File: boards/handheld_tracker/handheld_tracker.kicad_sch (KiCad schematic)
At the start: 0 parts

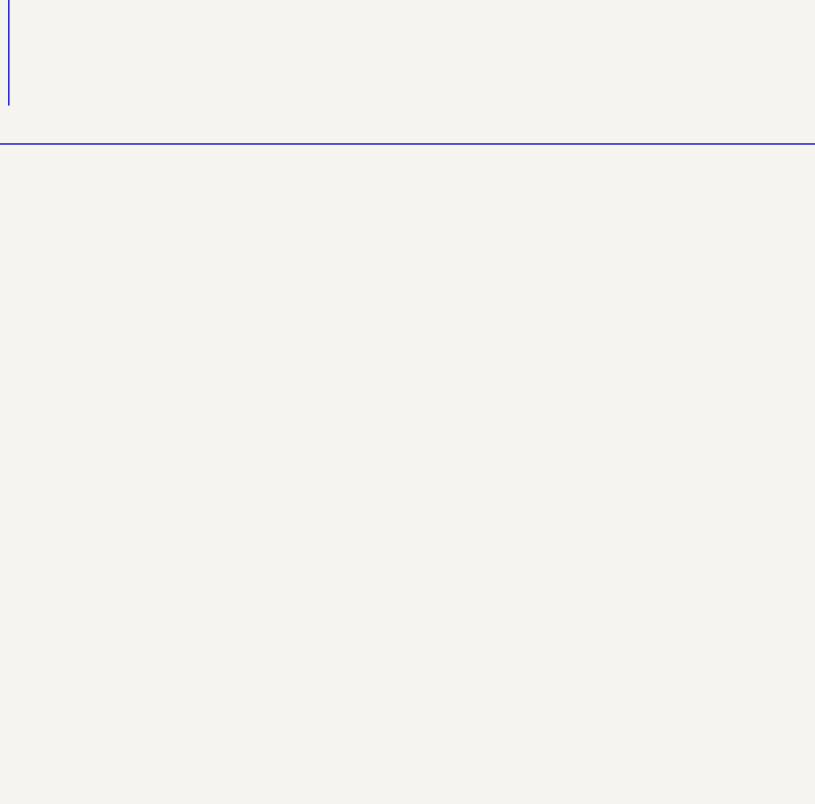
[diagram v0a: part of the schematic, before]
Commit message: created section for test pins
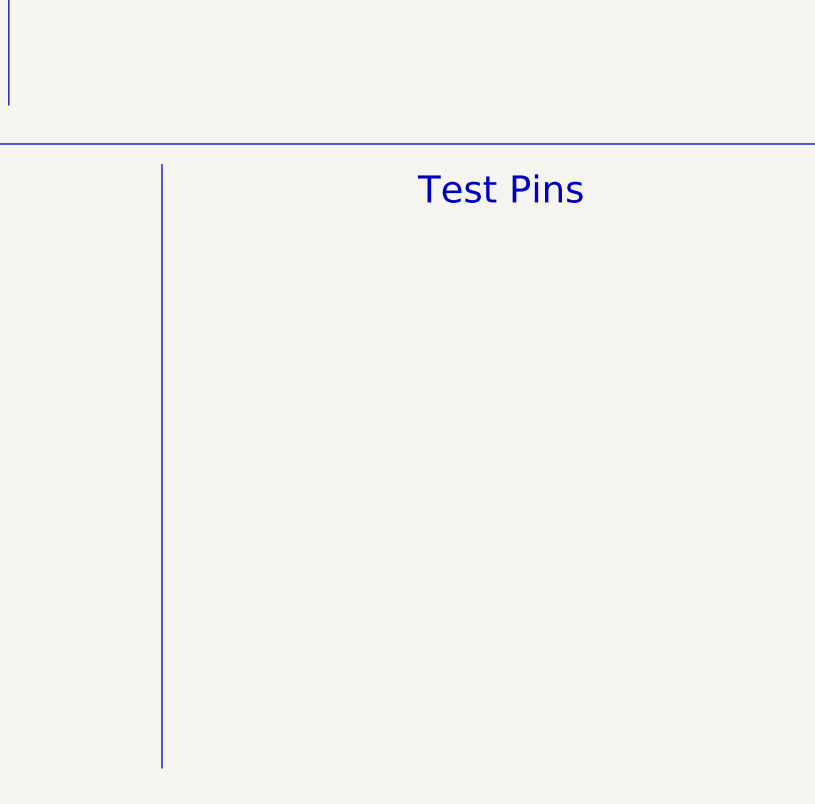
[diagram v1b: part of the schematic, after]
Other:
- note added: "Test Pins"
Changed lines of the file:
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@@
+    (stroke (width 0) (type default) (color 0 0 0 0))
+  )
+  (polyline (pts (xy 184.658 98.806) (xy 184.658 165.862))
     (stroke (width 0) (type default) (color 0 0 0 0))
   )
@@
     (effects (font (size 3 3)) (justify left bottom))
   )
+  (text "Test Pins" (at 213.106 103.632 0)
+    (effects (font (size 3 3)) (justify left bottom))
+  )

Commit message: added notes
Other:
- note added: "- I2C lines - SPI lines - Input voltage - Regulated voltage - GND"
- note added: "Likely needs to be modified to account for MCU change...may need 5V to power larger MCU"
- note added: "Make heirarchy...for buttons & screen"
- note added: "SAM-M8Q"
- note added: "TBD"
- note added: "Transceiver + SMA antenna connector"
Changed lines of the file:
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@@
     (effects (font (size 3 3)) (justify left bottom))
+  )
+  (text "Likely needs to be modified to account for MCU \nchange...may need 5V to power larger MCU"
+    (at 26.67 114.554 0)
+    (effects (font (size 1.27 1.27)) (justify left bottom))
   )
   (text "Test Pins" (at 213.106 103.632 0)
@@
     (effects (font (size 3 3)) (justify left bottom))
   )
+  (text "Transceiver + SMA antenna connector" (at 194.818 49.022 0)
+    (effects (font (size 1.27 1.27)) (justify left bottom))
+  )
+  (text "SAM-M8Q" (at 113.538 50.038 0)
+    (effects (font (size 1.27 1.27)) (justify left bottom))
+  )
+  (text "- I2C lines\n- SPI lines\n- Input voltage\n- Regulated voltage\n- GND"
+    (at 221.488 128.016 0)
+    (effects (font (size 1.27 1.27)) (justify left bottom))
+  )
+  (text "TBD" (at 42.672 52.324 0)
+    (effects (font (size 1.27 1.27)) (justify left bottom))
+  )
   (text "Power" (at 44.196 104.14 0)
     (effects (font (size 3 3)) (justify left bottom))
   )
+  (text "Make heirarchy...for buttons & screen" (at 118.618 125.73 0)
+    (effects (font (size 1.27 1.27)) (justify left bottom))
+  )
   (sheet_instances

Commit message: added sensor and MCU
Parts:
- added U1: SAM-M8Q, RF_GPS:ublox_SAM-M8Q, symbol RF_GPS:SAM-M8Q
- added U2: RFM96W-433S2, symbol RF_Module:RFM96W-433S2
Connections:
- new net: U1.1 (GND), U1.10 (GND), U1.11 (GND), U1.15 (GND), U1.16 (GND), U1.20 (GND), U1.4 (GND), U1.5 (GND), U1.6 (GND)
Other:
- added sheet mcu (mcu.kicad_sch)
- added sheet user_interface (user_interface.kicad_sch)
- note removed: "Likely needs to be modified to account for MCU change...may need 5V to power larger MCU"
- note removed: "Make heirarchy...for buttons & screen"
- note removed: "SAM-M8Q"
- note removed: "TBD"
- note removed: "Transceiver + SMA antenna connector"
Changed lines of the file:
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@@
     (stroke (width 0) (type default) (color 0 0 0 0))
   )
-  (text "MCU" (at 46.228 25.4 0)
+  (text "MCU" (at 45.72 25.4 0)
     (effects (font (size 3 3)) (justify left bottom))
   )
-  (text "Likely needs to be modified to account for MCU \nchange...may need 5V to power larger MCU"
-    (at 26.67 114.554 0)
+  (text "Test Pins" (at 214.63 104.14 0)
+    (effects (font (size 3 3)) (justify left bottom))
+  )
+  (text "User Interface" (at 114.3 105.41 0)
+    (effects (font (size 3 3)) (justify left bottom))
+  )
+  (text "Sensors" (at 118.11 24.13 0)
+    (effects (font (size 3 3)) (justify left bottom))
+  )
+  (text "Communication" (at 189.23 26.67 0)
+    (effects (font (size 3 3)) (justify left bottom))
+  )
+  (text "- I2C lines\n- SPI lines\n- Input voltage\n- Regulated voltage\n- GND"
+    (at 220.98 128.27 0)
     (effects (font (size 1.27 1.27)) (justify left bottom))
   )
-  (text "Test Pins" (at 213.106 103.632 0)
+  (text "Power" (at 44.45 105.41 0)
     (effects (font (size 3 3)) (justify left bottom))
   )
-  (text "User Interface" (at 114.3 104.394 0)
-    (effects (font (size 3 3)) (justify left bottom))
+  (symbol (lib_id "RF_Module:RFM96W-433S2") (at 213.36 52.07 0) (unit 1)
+    (in_bom yes) (on_board yes) (fields_autoplaced)
+    (property "Reference" "U2" (id 0) (at 215.3794 37.084 0)
+      (effects (font (size 1.27 1.27)) (justify left))
+    )
+    (property "Value" "RFM96W-433S2" (id 1) (at 215.3794 39.624 0)
+      (effects (font (size 1.27 1.27)) (justify left))
+    )
+    (property "Footprint" "" (id 2) (at 129.54 10.16 0)
+      (effects (font (size 1.27 1.27)) hide)
+    )
+    (property "Datasheet" "https://www.hoperf.com/data/upload/portal/20181127/5bfcc0ac60235.pdf" (id 3) (at 129.54 10.16 0)
+      (effects (font (size 1.27 1.27)) hide)
+    )
+    (pin "1")
+    (pin "10")
+    (pin "11")
+    (pin "12")
+    (pin "13")
+    (pin "14")
+    (pin "15")
+    (pin "16")
+    (pin "2")
+    (pin "3")
+    (pin "4")
+    (pin "5")
+    (pin "6")
+    (pin "7")
+    (pin "8")
+    (pin "9")
   )
-  (text "Sensors" (at 118.872 25.146 0)
-    (effects (font (size 3 3)) (justify left bottom))
+  (symbol (lib_id "RF_GPS:SAM-M8Q") (at 128.27 54.61 0) (unit 1)
+    (in_bom yes) (on_board yes) (fields_autoplaced)
+    (property "Reference" "U1" (id 0) (at 130.2894 67.564 0)
+      (effects (font (size 1.27 1.27)) (justify left))
+    )
+    (property "Value" "SAM-M8Q" (id 1) (at 130.2894 70.104 0)
+      (effects (font (size 1.27 1.27)) (justify left))
+    )
+    (property "Footprint" "RF_GPS:ublox_SAM-M8Q" (id 2) (at 140.97 66.04 0)
+      (effects (font (size 1.27 1.27)) hide)
+    )
+    (property "Datasheet" "https://www.u-blox.com/sites/default/files/SAM-M8Q_DataSheet_%28UBX-16012619%29.pdf" (id 3) (at 128.27 54.61 0)
+      (effects (font (size 1.27 1.27)) hide)
+    )
+    (pin "1")
+    (pin "10")
+    (pin "11")
+    (pin "12")
+    (pin "13")
+    (pin "14")
+    (pin "15")
+    (pin "16")
+    (pin "17")
+    (pin "18")
+    (pin "19")
+    (pin "2")
+    (pin "20")
+    (pin "3")
+    (pin "4")
+    (pin "5")
+    (pin "6")
+    (pin "7")
+    (pin "8")
+    (pin "9")
   )
-  (text "Communication" (at 188.976 25.4 0)
-    (effects (font (size 3 3)) (justify left bottom))
+  (sheet (at 31.75 32.512) (size 48.26 43.688) (fields_autoplaced)
+    (stroke (width 0.1524) (type solid) (color 0 0 0 0))
+    (fill (color 0 0 0 0.0000))
+    (property "Sheet name" "mcu" (id 0) (at 31.75 31.8004 0)
+      (effects (font (size 1.27 1.27)) (justify left bottom))
+    )
+    (property "Sheet file" "mcu.kicad_sch" (id 1) (at 31.75 76.7846 0)
+      (effects (font (size 1.27 1.27)) (justify left top))
+    )
   )
-  (text "Transceiver + SMA antenna connector" (at 194.818 49.022 0)
-    (effects (font (size 1.27 1.27)) (justify left bottom))
-  )
-  (text "SAM-M8Q" (at 113.538 50.038 0)
-    (effects (font (size 1.27 1.27)) (justify left bottom))
-  )
-  (text "- I2C lines\n- SPI lines\n- Input voltage\n- Regulated voltage\n- GND"
-    (at 221.488 128.016 0)
-    (effects (font (size 1.27 1.27)) (justify left bottom))
-  )
-  (text "TBD" (at 42.672 52.324 0)
-    (effects (font (size 1.27 1.27)) (justify left bottom))
-  )
-  (text "Power" (at 44.196 104.14 0)
-    (effects (font (size 3 3)) (justify left bottom))
-  )
-  (text "Make heirarchy...for buttons & screen" (at 118.618 125.73 0)
-    (effects (font (size 1.27 1.27)) (justify left bottom))
+  (sheet (at 105.664 112.268) (size 58.928 41.402) (fields_autoplaced)
+    (stroke (width 0.1524) (type solid) (color 0 0 0 0))
+    (fill (color 0 0 0 0.0000))
+    (property "Sheet name" "user_interface" (id 0) (at 105.664 111.5564 0)
+      (effects (font (size 1.27 1.27)) (justify left bottom))
+    )
+    (property "Sheet file" "user_interface.kicad_sch" (id 1) (at 105.664 154.2546 0)
+      (effects (font (size 1.27 1.27)) (justify left top))
+    )
   )
   (sheet_instances
     (path "/" (page "1"))
+    (path "/b5768583-2921-450f-a3c7-6bb918f05112" (page "2"))
+    (path "/b8ad5378-5a94-4f95-a07b-9b83e4a5ed8b" (page "3"))
+  )
+  (symbol_instances
+    (path "/b5768583-2921-450f-a3c7-6bb918f05112/06cc3fef-5a0f-4290-a494-d4a8010342f4"
+      (reference "#PWR01") (unit 1) (value "GND") (footprint "")
+    )
+    (path "/b5768583-2921-450f-a3c7-6bb918f05112/cb9cf507-c2c8-48a7-ba33-3e774db067f2"
+      (reference "#PWR02") (unit 1) (value "+3.3V") (footprint "")
+    )
+    (path "/b5768583-2921-450f-a3c7-6bb918f05112/8c0bfa28-e8df-4e57-b5ab-4fdc05fdcaac"
+      (reference "#PWR03") (unit 1) (value "GND") (footprint "")
+    )
+    (path "/b5768583-2921-450f-a3c7-6bb918f05112/877f679f-dfe0-49aa-9685-3d35fb647b05"
+      (reference "#PWR04") (unit 1) (value "GND") (footprint "")
+    )
+    (path "/b5768583-2921-450f-a3c7-6bb918f05112/beb4de5e-8286-4b90-a981-aaa36965d340"
+      (reference "C1") (unit 1) (value "100nF") (footprint "")
+    )
+    (path "/b5768583-2921-450f-a3c7-6bb918f05112/351d2739-d309-4573-a07d-5b8b1db39041"
+      (reference "C2") (unit 1) (value "22pF") (footprint "")
+    )
+    (path "/b5768583-2921-450f-a3c7-6bb918f05112/a29b3cc5-b4af-44ca-86c6-432bb12f8887"
+      (reference "C3") (unit 1) (value "22pF") (footprint "")
+    )
+    (path "/b5768583-2921-450f-a3c7-6bb918f05112/a4753933-53f9-4d3f-8b8d-fe28a85e8bcb"
+      (reference "R1") (unit 1) (value "1K") (footprint "")
+    )
+    (path "/b5768583-2921-450f-a3c7-6bb918f05112/27cfb03c-4ae6-41c4-8bc1-a4ee468d77c0"
+      (reference "R2") (unit 1) (value "1K") (footprint "")
+    )
+    (path "/b598cb7e-54f3-46ef-9ba0-cbca9c5afa76"
+      (reference "U1") (unit 1) (value "SAM-M8Q") (footprint "RF_GPS:ublox_SAM-M8Q")
+    )
+    (path "/8ef8a62b-b263-4cfe-9734-b1f019360e3e"
+      (reference "U2") (unit 1) (value "RFM96W-433S2") (footprint "")
+    )
+    (path "/b5768583-2921-450f-a3c7-6bb918f05112/3c6ad485-bc99-421d-ab6a-7a36d0ebf7c0"
+      (reference "U3") (unit 1) (value "ATmega328PB-A") (footprint "Package_QFP:TQFP-32_7x7mm_P0.8mm")
+    )
+    (path "/b5768583-2921-450f-a3c7-6bb918f05112/220bb792-af47-49da-8cc5-89208b5293aa"
+      (reference "Y1") (unit 1) (value "Crystal") (footprint "")
+    )
   )
 )

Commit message: added manas hanheld tracker edits
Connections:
- net GND: now reaches U2.1 (GND)
- net GND: now also U2.10 (GND), U2.8 (GND)
- net +3.3V: now reaches U2.13 (3.3V)
- net MISO (from MCU): now reaches U2.2 (MISO)
- net MOSI (from MCU): now reaches U2.3 (MOSI)
- net SCK (from MCU): now reaches U2.4 (SCK)
- net CS: now reaches U2.5 (NSS)
- net RESET: now reaches U2.6 (RESET)

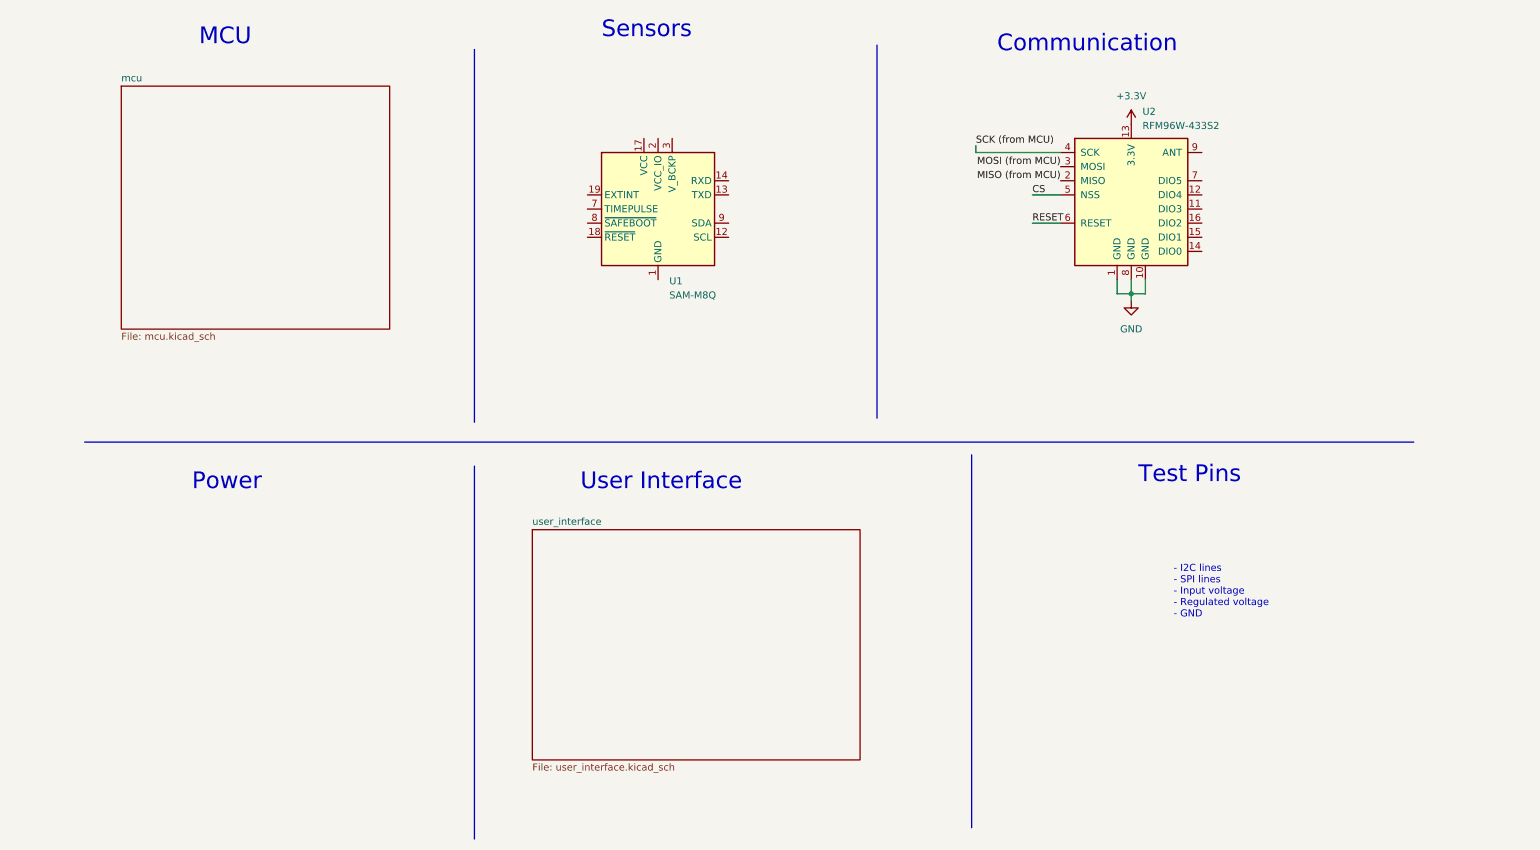
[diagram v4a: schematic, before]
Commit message: added test pads, UI buttons, and routed MCU pins
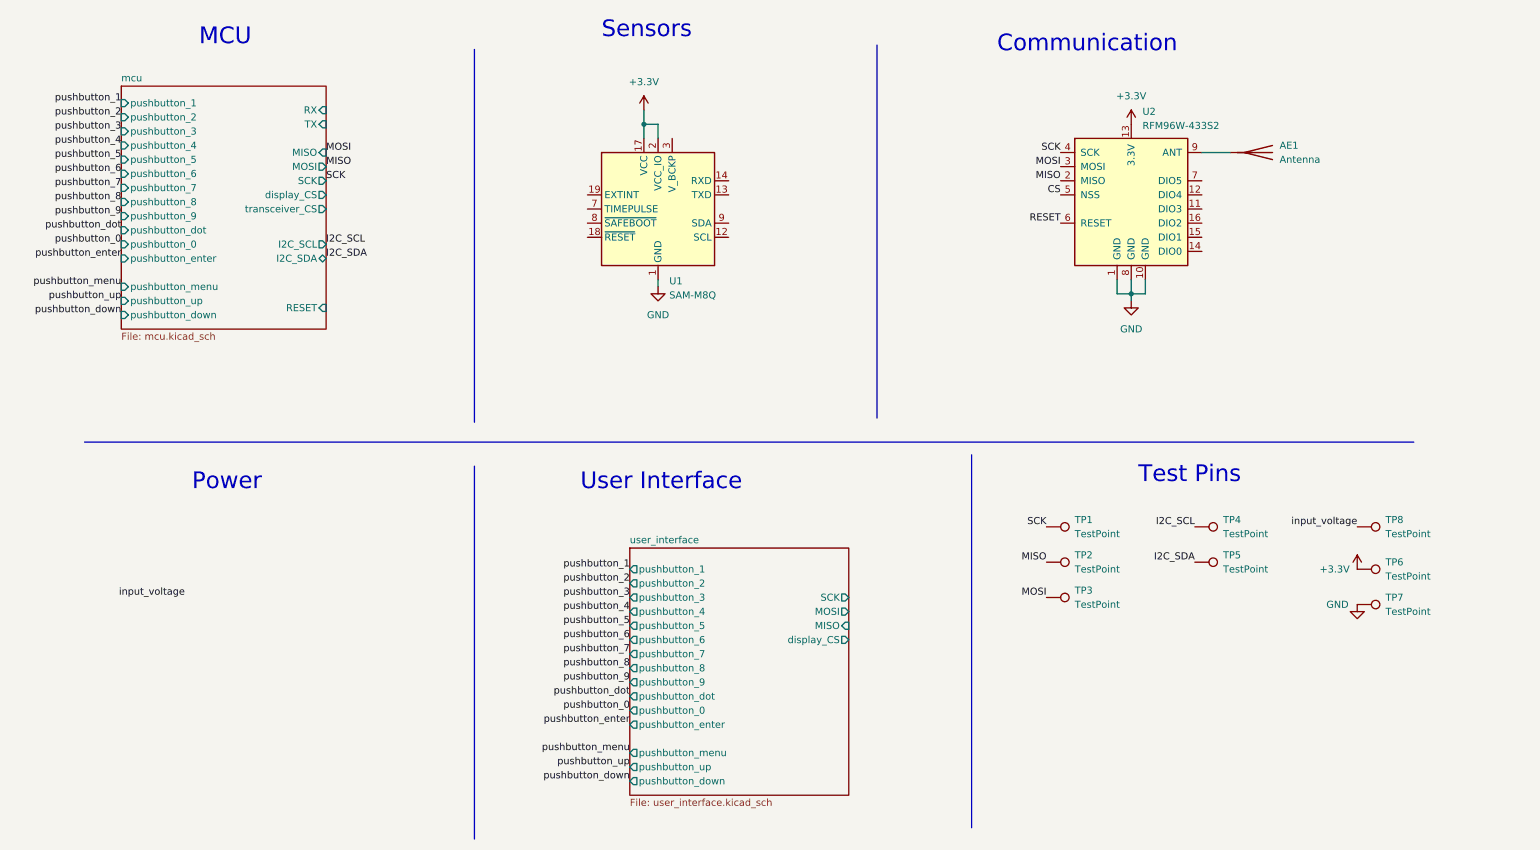
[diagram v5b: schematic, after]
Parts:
- added AE1: Antenna, symbol Device:Antenna
- added TP1, TP2, TP3, TP4, TP5, TP6, TP7, TP8: TestPoint, TestPoint:TestPoint_Pad_D3.0mm, symbol Connector:TestPoint
- U2: footprint (none) -> RF_Module:HOPERF_RFM9XW_THT
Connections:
- net +3.3V: now also U1.17 (VCC), U1.2 (VCC_IO), TP6.1
- net GND: now also U1.1 (GND), U1.10 (GND), U1.11 (GND), U1.15 (GND), U1.16 (GND), U1.20 (GND), U1.4 (GND), U1.5 (GND), U1.6 (GND), TP7.1
- net at U2.9 (ANT): now also AE1.1 (A)
- net MISO (from MCU) renamed MISO
- net MISO: now also TP2.1
- net MOSI (from MCU) renamed MOSI
- net MOSI: now also TP3.1
- net SCK (from MCU) renamed SCK
- net SCK: now also TP1.1
- new net I2C_SCL: TP4.1
- new net I2C_SDA: TP5.1
- new net input_voltage: TP8.1
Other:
- sheet mcu ports: added I2C_SCL, I2C_SDA, MISO, MOSI, RESET, RX, SCK, TX, display_CS, pushbutton_0, pushbutton_1, pushbutton_2, pushbutton_3, pushbutton_4, pushbutton_5, pushbutton_6, pushbutton_7, pushbutton_8, pushbutton_9, pushbutton_dot, pushbutton_down, pushbutton_enter, pushbutton_menu, pushbutton_up, transceiver_CS; removed none
- sheet user_interface ports: added MISO, MOSI, SCK, display_CS, pushbutton_0, pushbutton_1, pushbutton_2, pushbutton_3, pushbutton_4, pushbutton_5, pushbutton_6, pushbutton_7, pushbutton_8, pushbutton_9, pushbutton_dot, pushbutton_down, pushbutton_enter, pushbutton_menu, pushbutton_up; removed none
- note removed: "- I2C lines - SPI lines - Input voltage - Regulated voltage - GND"

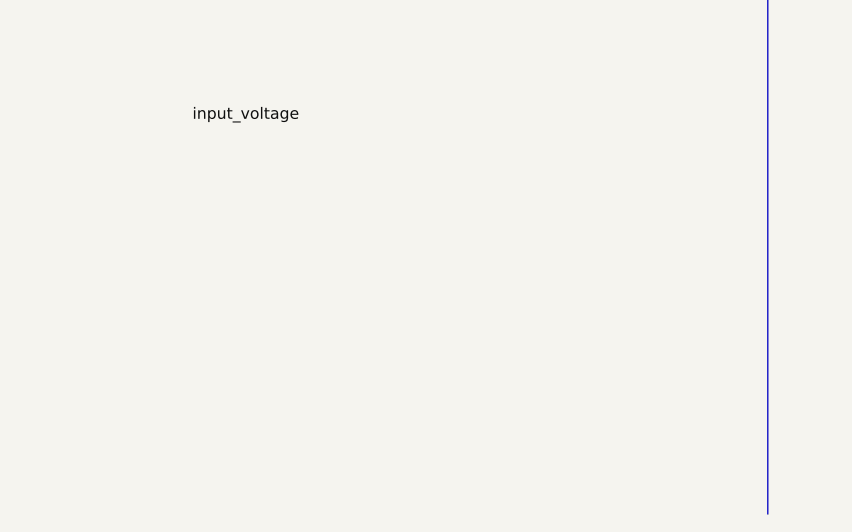
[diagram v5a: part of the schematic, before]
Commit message: buck placed on sch
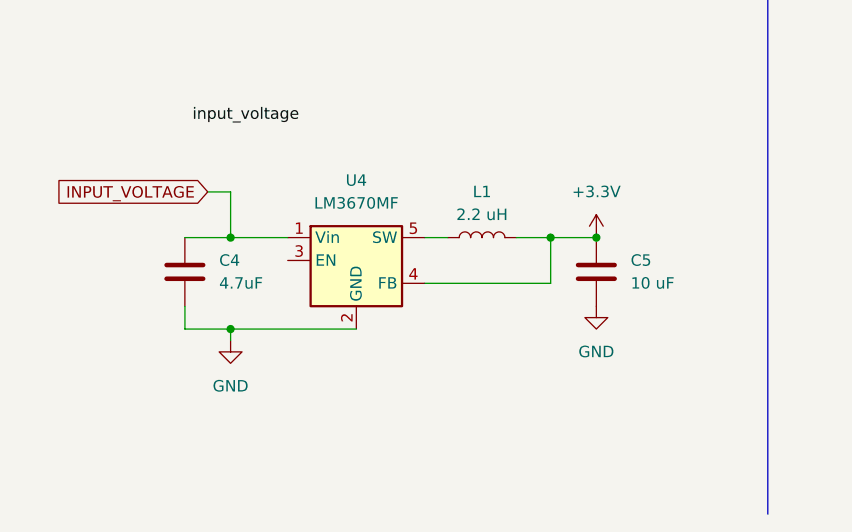
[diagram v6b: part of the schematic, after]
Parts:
- added C4: 4.7uF, symbol Device:C
- added C5: 10 uF, symbol Device:C
- added L1: 2.2 uH, symbol Device:L
- added U4: LM3670MF, Package_TO_SOT_SMD:TSOT-23-5, symbol Regulator_Switching:LM3670MF
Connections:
- net +3.3V: now also C5.1, L1.2, U4.4 (FB)
- net GND: now also C4.2, C5.2, U4.2 (GND)
- new net: L1.1, U4.5 (SW)
- new net INPUT_VOLTAGE: C4.1, U4.1 (Vin)
